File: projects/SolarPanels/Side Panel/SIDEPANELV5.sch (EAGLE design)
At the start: 31 parts

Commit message: Side Panel V5 Finished (?)
Ready to be checked
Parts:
- added 8A, 8B, 8C, 8D: SOLARCELLV3, BrownSpaceEngineering:SOLARCELLV3
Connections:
- net 2C renamed N$5
- new net N$23: 8C.C, 8D.A
- new net N$24: 8B.C, 8C.A
- new net N$25: 8A.C, 8B.A
- net GND: now also 8A.A
- net PWR-OUT: now also 8D.C
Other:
- moved on the sheet: 1A, 1B, 1C, 1D, 2A, 2B, 2C, 2D, 3A, 3B, 3C, 3D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

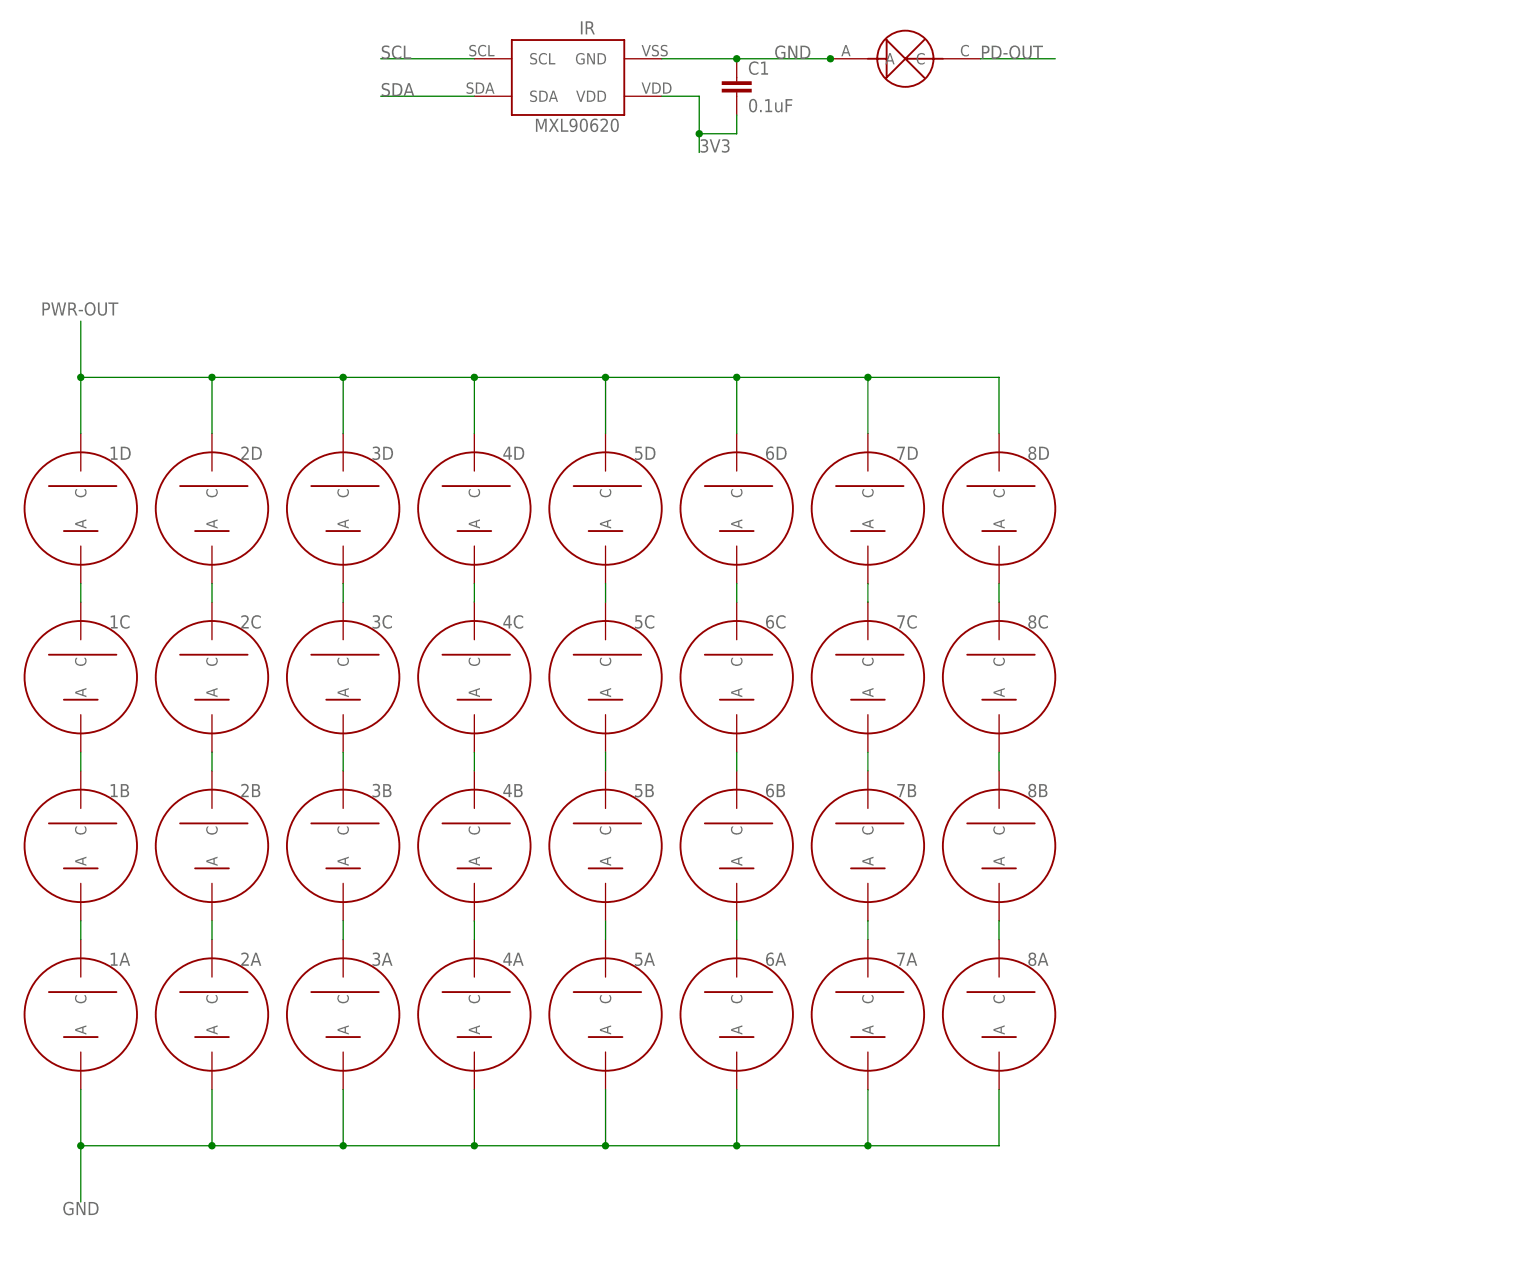
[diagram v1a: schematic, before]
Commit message: Side Panel V5 In Review (Part Deux)
Fixed the things Ryan commented on.
Warning: back of via 1D will need to be taped as the board is now!
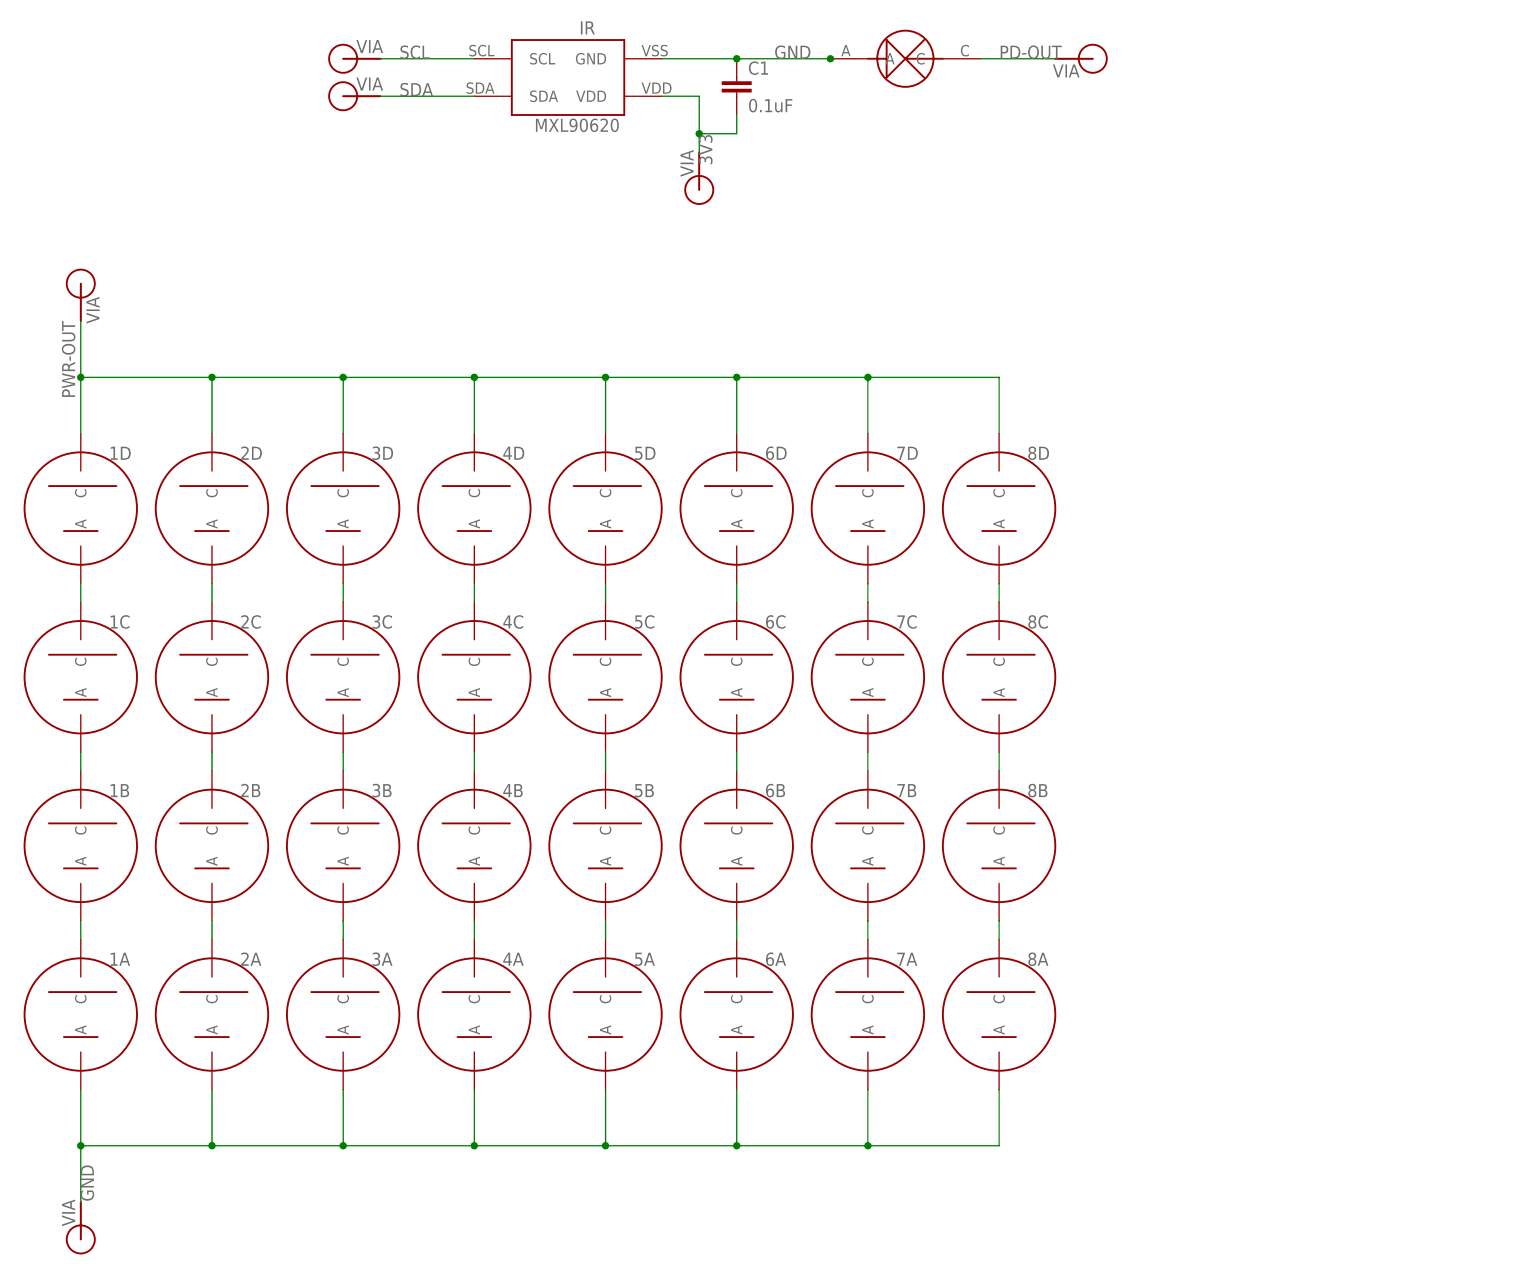
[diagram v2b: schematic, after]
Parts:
- added 3V3, GND, PD-OUT, PWR-OUT, SCL, SDA: (no value), BrownSpaceEngineering:VIA60MIL-SQ
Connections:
- net 3V3: now also 3V3.P$1
- net GND: now also GND.P$1
- net PD-OUT: now also PD-OUT.P$1
- net PWR-OUT: now also PWR-OUT.P$1
- net SCL: now also SCL.P$1
- net SDA: now also SDA.P$1
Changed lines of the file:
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@@
 <part name="8B" library="BrownSpaceEngineering" deviceset="SOLARCELLV3" device=""/>
 <part name="8A" library="BrownSpaceEngineering" deviceset="SOLARCELLV3" device=""/>
+<part name="SCL" library="BrownSpaceEngineering" deviceset="VIA" device="60MIL-SQ"/>
+<part name="SDA" library="BrownSpaceEngineering" deviceset="VIA" device="60MIL-SQ"/>
+<part name="PD-OUT" library="BrownSpaceEngineering" deviceset="VIA" device="60MIL-SQ"/>
+<part name="3V3" library="BrownSpaceEngineering" deviceset="VIA" device="60MIL-SQ"/>
+<part name="PWR-OUT" library="BrownSpaceEngineering" deviceset="VIA" device="60MIL-SQ"/>
+<part name="GND" library="BrownSpaceEngineering" deviceset="VIA" device="60MIL-SQ"/>
 </parts>
 <sheets>
@@
 <instance part="8B" gate="G$1" x="-20.32" y="0"/>
 <instance part="8A" gate="G$1" x="-20.32" y="-22.86"/>
+<instance part="SCL" gate="G$1" x="-109.22" y="106.68"/>
+<instance part="SDA" gate="G$1" x="-109.22" y="101.6"/>
+<instance part="PD-OUT" gate="G$1" x="-7.62" y="106.68" rot="R180"/>
+<instance part="3V3" gate="G$1" x="-60.96" y="88.9" rot="R90"/>
+<instance part="PWR-OUT" gate="G$1" x="-144.78" y="76.2" rot="R270"/>
+<instance part="GND" gate="G$1" x="-144.78" y="-53.34" rot="R90"/>
 </instances>
 <busses>
@@
 <pinref part="1A" gate="G$1" pin="A"/>
 <wire x1="-144.78" y1="-33.02" x2="-144.78" y2="-40.64" width="0.1524" layer="91"/>
-<label x="-142.24" y="-48.26" size="1.778" layer="95" rot="R180"/>
+<label x="-144.78" y="-43.18" size="1.778" layer="95" rot="R270"/>
 <wire x1="-20.32" y1="-40.64" x2="-38.1" y2="-40.64" width="0.1524" layer="91"/>
 <pinref part="7A" gate="G$1" pin="A"/>
@@
 <wire x1="-144.78" y1="-40.64" x2="-144.78" y2="-48.26" width="0.1524" layer="91"/>
 <junction x="-144.78" y="-40.64"/>
+<pinref part="GND" gate="G$1" pin="P$1"/>
 </segment>
 </net>
@@
 <pinref part="IR" gate="G$1" pin="SDA"/>
 <wire x1="-91.44" y1="101.6" x2="-104.14" y2="101.6" width="0.1524" layer="91"/>
-<label x="-104.14" y="101.6" size="1.778" layer="95"/>
+<label x="-101.6" y="101.6" size="1.778" layer="95"/>
+<pinref part="SDA" gate="G$1" pin="P$1"/>
 </segment>
 </net>
@@
 <pinref part="IR" gate="G$1" pin="SCL"/>
 <wire x1="-91.44" y1="106.68" x2="-104.14" y2="106.68" width="0.1524" layer="91"/>
-<label x="-104.14" y="106.68" size="1.778" layer="95"/>
+<label x="-101.6" y="106.68" size="1.778" layer="95"/>
+<pinref part="SCL" gate="G$1" pin="P$1"/>
 </segment>
 </net>
@@
 <wire x1="-55.88" y1="96.52" x2="-55.88" y2="99.06" width="0.1524" layer="91"/>
 <junction x="-60.96" y="96.52"/>
-<label x="-60.96" y="93.98" size="1.778" layer="95"/>
+<label x="-60.96" y="96.52" size="1.778" layer="95" rot="R270"/>
+<pinref part="3V3" gate="G$1" pin="P$1"/>
 </segment>
 </net>
@@
 <pinref part="PD" gate="G$1" pin="C"/>
 <wire x1="-22.86" y1="106.68" x2="-12.7" y2="106.68" width="0.1524" layer="91"/>
-<label x="-22.86" y="106.68" size="1.778" layer="95"/>
+<label x="-20.32" y="106.68" size="1.778" layer="95"/>
+<pinref part="PD-OUT" gate="G$1" pin="P$1"/>
 </segment>
 </net>
@@
 <pinref part="1D" gate="G$1" pin="C"/>
 <wire x1="-144.78" y1="55.88" x2="-144.78" y2="63.5" width="0.1524" layer="91"/>
-<label x="-139.7" y="73.66" size="1.778" layer="95" rot="R180"/>
+<label x="-147.32" y="71.12" size="1.778" layer="95" rot="R270"/>
 <wire x1="-127" y1="63.5" x2="-144.78" y2="63.5" width="0.1524" layer="91"/>
 <wire x1="-109.22" y1="63.5" x2="-127" y2="63.5" width="0.1524" layer="91"/>
@@
 <wire x1="-144.78" y1="63.5" x2="-144.78" y2="71.12" width="0.1524" layer="91"/>
 <junction x="-144.78" y="63.5"/>
-</segment>
-</net>
+<pinref part="PWR-OUT" gate="G$1" pin="P$1"/>
+</segment>
+</net>

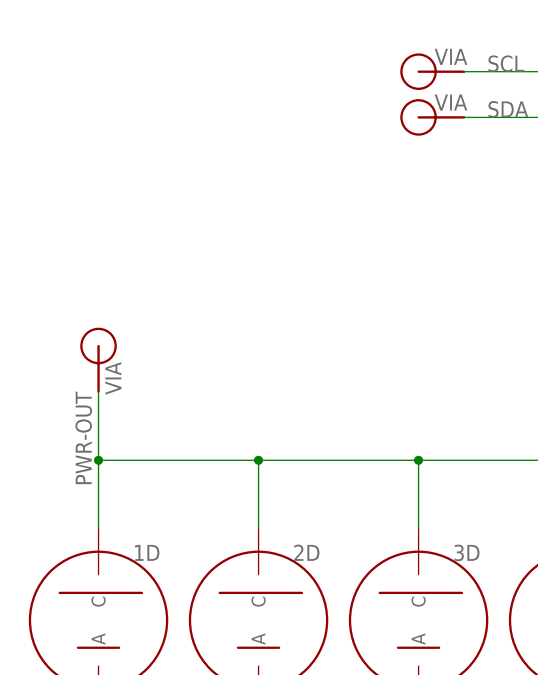
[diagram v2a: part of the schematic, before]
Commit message: Side Panel V5 In Review (Part III)
>  Added diode and 0R resistor in parallel between the cells' output and
PWR-OUT (this circuit is being moved from Battery Board V1).
>  Top layer is now the CELL-OUT signal.
>  Put C1 on bottom layer.
>  Moved all the vias further away from the cells.
>  Connected the corner screw holes to GND.
>  Readjusted exposed copper pads to cover chassis rails and tabs with
~0.5 mm extra space on all sides.
>  Shifted all components slightly left so that 1D is the only non-GND
via that will be in contact with the chassis (and thus will need to be
covered with insulating tape).
>  Fixed traces to come out of the cell pads perpindicularly.
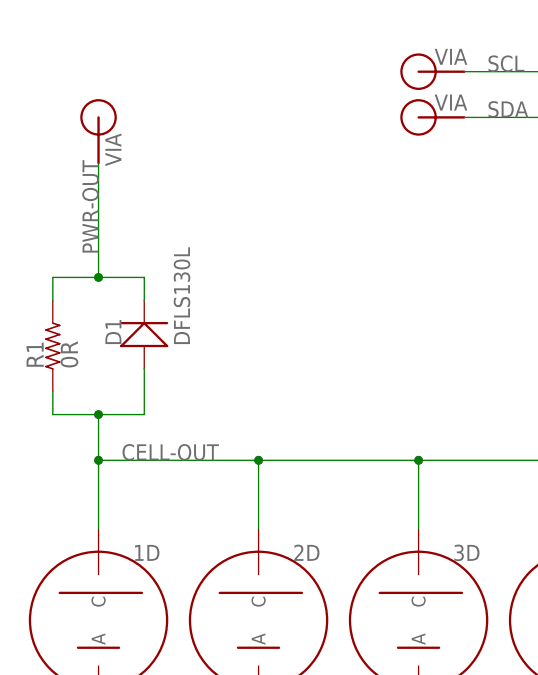
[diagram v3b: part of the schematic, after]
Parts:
- added D1: DFLS130L, BrownSpaceEngineering:DFLS130L
- added R1: 0R, BrownSpaceEngineering:RES1210
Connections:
- new net CELL-OUT: 1D.C, 2D.C, 3D.C, 4D.C, 5D.C, 6D.C, 7D.C, 8D.C, D1.A, R1.1
- net PWR-OUT: now also D1.C, R1.2; no longer 1D.C, 2D.C, 3D.C, 4D.C, 5D.C, 6D.C, 7D.C, 8D.C
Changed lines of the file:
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@@
 <part name="PWR-OUT" library="BrownSpaceEngineering" deviceset="VIA" device="60MIL-SQ"/>
 <part name="GND" library="BrownSpaceEngineering" deviceset="VIA" device="60MIL-SQ"/>
+<part name="D1" library="BrownSpaceEngineering" deviceset="DFLS130L" device="" value="DFLS130L"/>
+<part name="R1" library="BrownSpaceEngineering" deviceset="RES" device="1210" value="0R"/>
 </parts>
 <sheets>
@@
 <instance part="PD-OUT" gate="G$1" x="-7.62" y="106.68" rot="R180"/>
 <instance part="3V3" gate="G$1" x="-60.96" y="88.9" rot="R90"/>
-<instance part="PWR-OUT" gate="G$1" x="-144.78" y="76.2" rot="R270"/>
+<instance part="PWR-OUT" gate="G$1" x="-144.78" y="101.6" smashed="yes" rot="R270">
+<attribute name="VALUE" x="-147.32" y="99.822" size="1.778" layer="96" rot="R270"/>
+</instance>
 <instance part="GND" gate="G$1" x="-144.78" y="-53.34" rot="R90"/>
+<instance part="D1" gate="G$1" x="-139.7" y="76.2" rot="R90"/>
+<instance part="R1" gate="R$1" x="-149.86" y="76.2" rot="R90"/>
 </instances>
 <busses>
@@
 </segment>
 </net>
-<net name="PWR-OUT" class="0">
+<net name="CELL-OUT" class="0">
 <segment>
 <pinref part="7D" gate="G$1" pin="C"/>
@@
 <pinref part="1D" gate="G$1" pin="C"/>
 <wire x1="-144.78" y1="55.88" x2="-144.78" y2="63.5" width="0.1524" layer="91"/>
-<label x="-147.32" y="71.12" size="1.778" layer="95" rot="R270"/>
 <wire x1="-127" y1="63.5" x2="-144.78" y2="63.5" width="0.1524" layer="91"/>
 <wire x1="-109.22" y1="63.5" x2="-127" y2="63.5" width="0.1524" layer="91"/>
@@
 <junction x="-55.88" y="63.5"/>
 <junction x="-38.1" y="63.5"/>
-<wire x1="-144.78" y1="63.5" x2="-144.78" y2="71.12" width="0.1524" layer="91"/>
 <junction x="-144.78" y="63.5"/>
+<wire x1="-144.78" y1="63.5" x2="-144.78" y2="68.58" width="0.1524" layer="91"/>
+<pinref part="D1" gate="G$1" pin="A"/>
+<wire x1="-144.78" y1="68.58" x2="-139.7" y2="68.58" width="0.1524" layer="91"/>
+<wire x1="-139.7" y1="68.58" x2="-139.7" y2="73.66" width="0.1524" layer="91"/>
+<junction x="-144.78" y="68.58"/>
+<pinref part="R1" gate="R$1" pin="1"/>
+<wire x1="-144.78" y1="68.58" x2="-149.86" y2="68.58" width="0.1524" layer="91"/>
+<wire x1="-149.86" y1="68.58" x2="-149.86" y2="71.12" width="0.1524" layer="91"/>
+<label x="-142.24" y="63.5" size="1.778" layer="95"/>
+</segment>
+</net>
+<net name="PWR-OUT" class="0">
+<segment>
+<pinref part="R1" gate="R$1" pin="2"/>
+<wire x1="-149.86" y1="81.28" x2="-149.86" y2="83.82" width="0.1524" layer="91"/>
+<pinref part="D1" gate="G$1" pin="C"/>
+<wire x1="-139.7" y1="81.28" x2="-139.7" y2="83.82" width="0.1524" layer="91"/>
+<wire x1="-139.7" y1="83.82" x2="-144.78" y2="83.82" width="0.1524" layer="91"/>
 <pinref part="PWR-OUT" gate="G$1" pin="P$1"/>
-</segment>
-</net>
+<wire x1="-144.78" y1="83.82" x2="-149.86" y2="83.82" width="0.1524" layer="91"/>
+<wire x1="-144.78" y1="83.82" x2="-144.78" y2="96.52" width="0.1524" layer="91"/>
+<junction x="-144.78" y="83.82"/>
+<label x="-144.78" y="86.36" size="1.778" layer="95" rot="R90"/>
+</segment>
+</net>
